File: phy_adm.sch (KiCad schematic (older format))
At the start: 28 parts

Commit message: sch: Add misc doc texts
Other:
- note added: "PHY reference clock"
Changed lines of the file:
@@
 Wire Wire Line
 	4500 5500 4500 5750
+Text Notes 4800 6400 0    50   ~ 0
+PHY reference clock
 $EndSCHEMATC

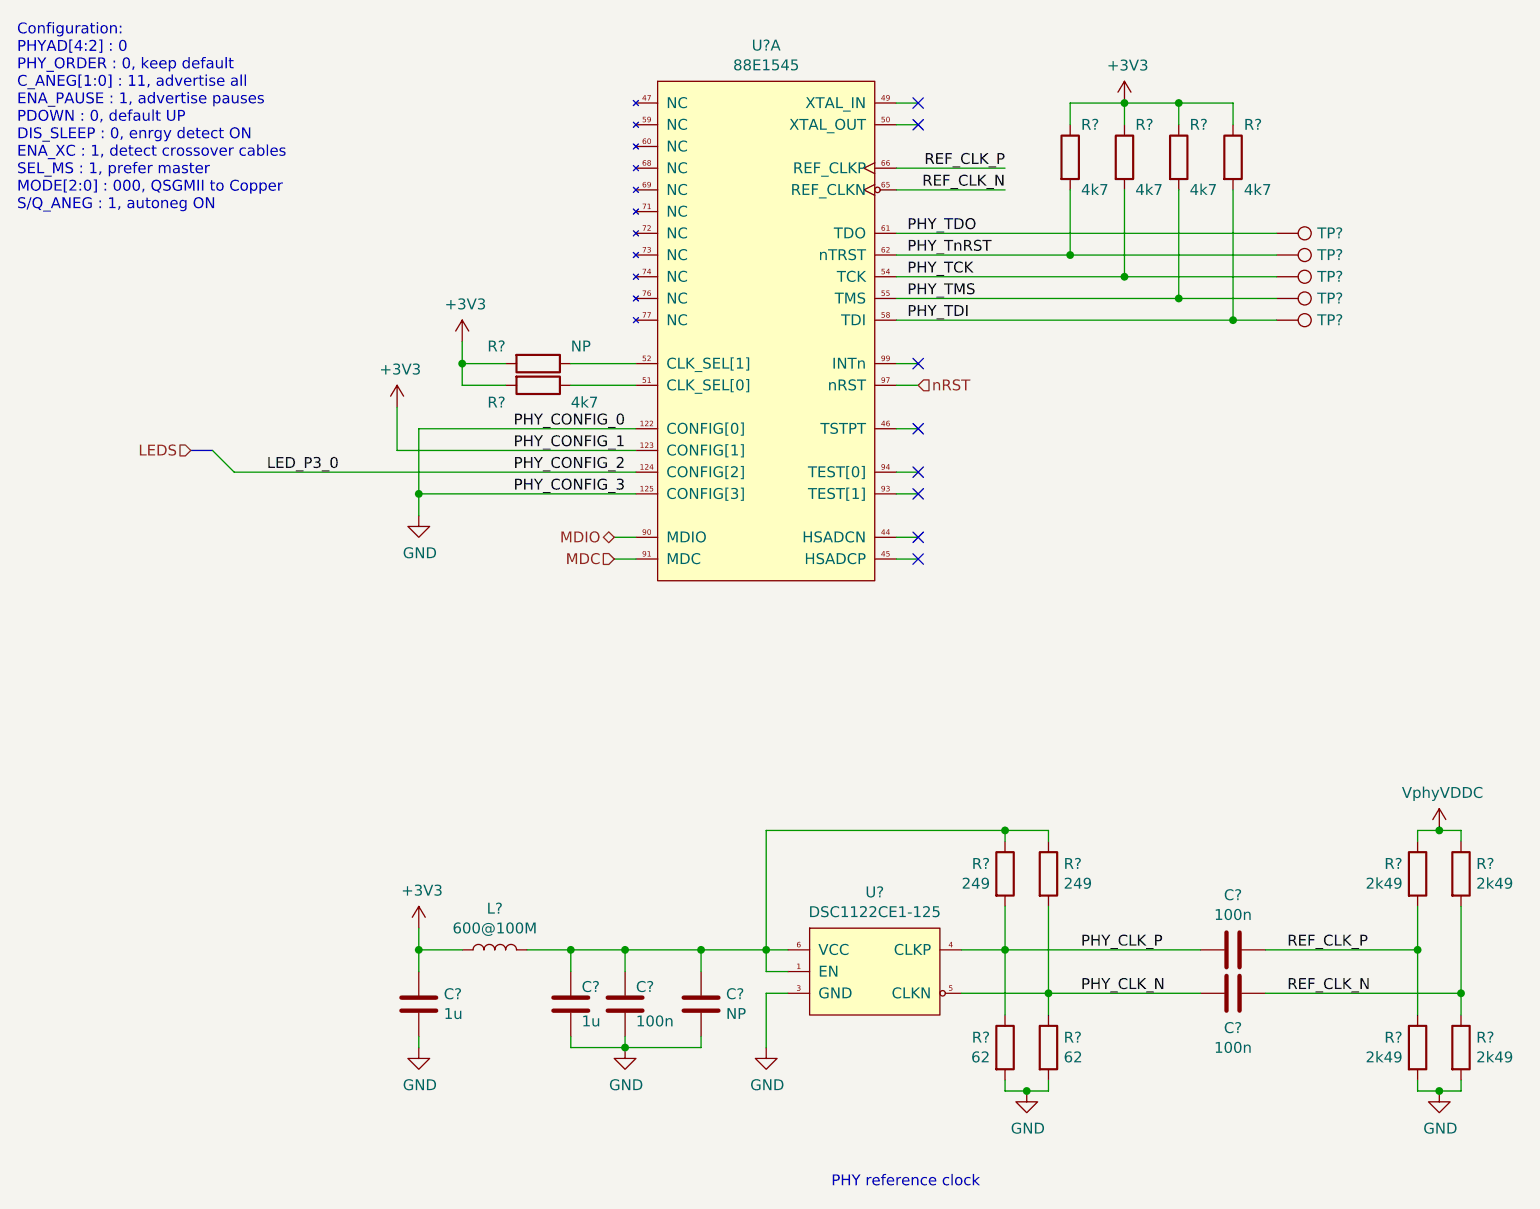
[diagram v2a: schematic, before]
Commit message: sch: Replace regular symbols with small variant
Done for most capacitors and resistors
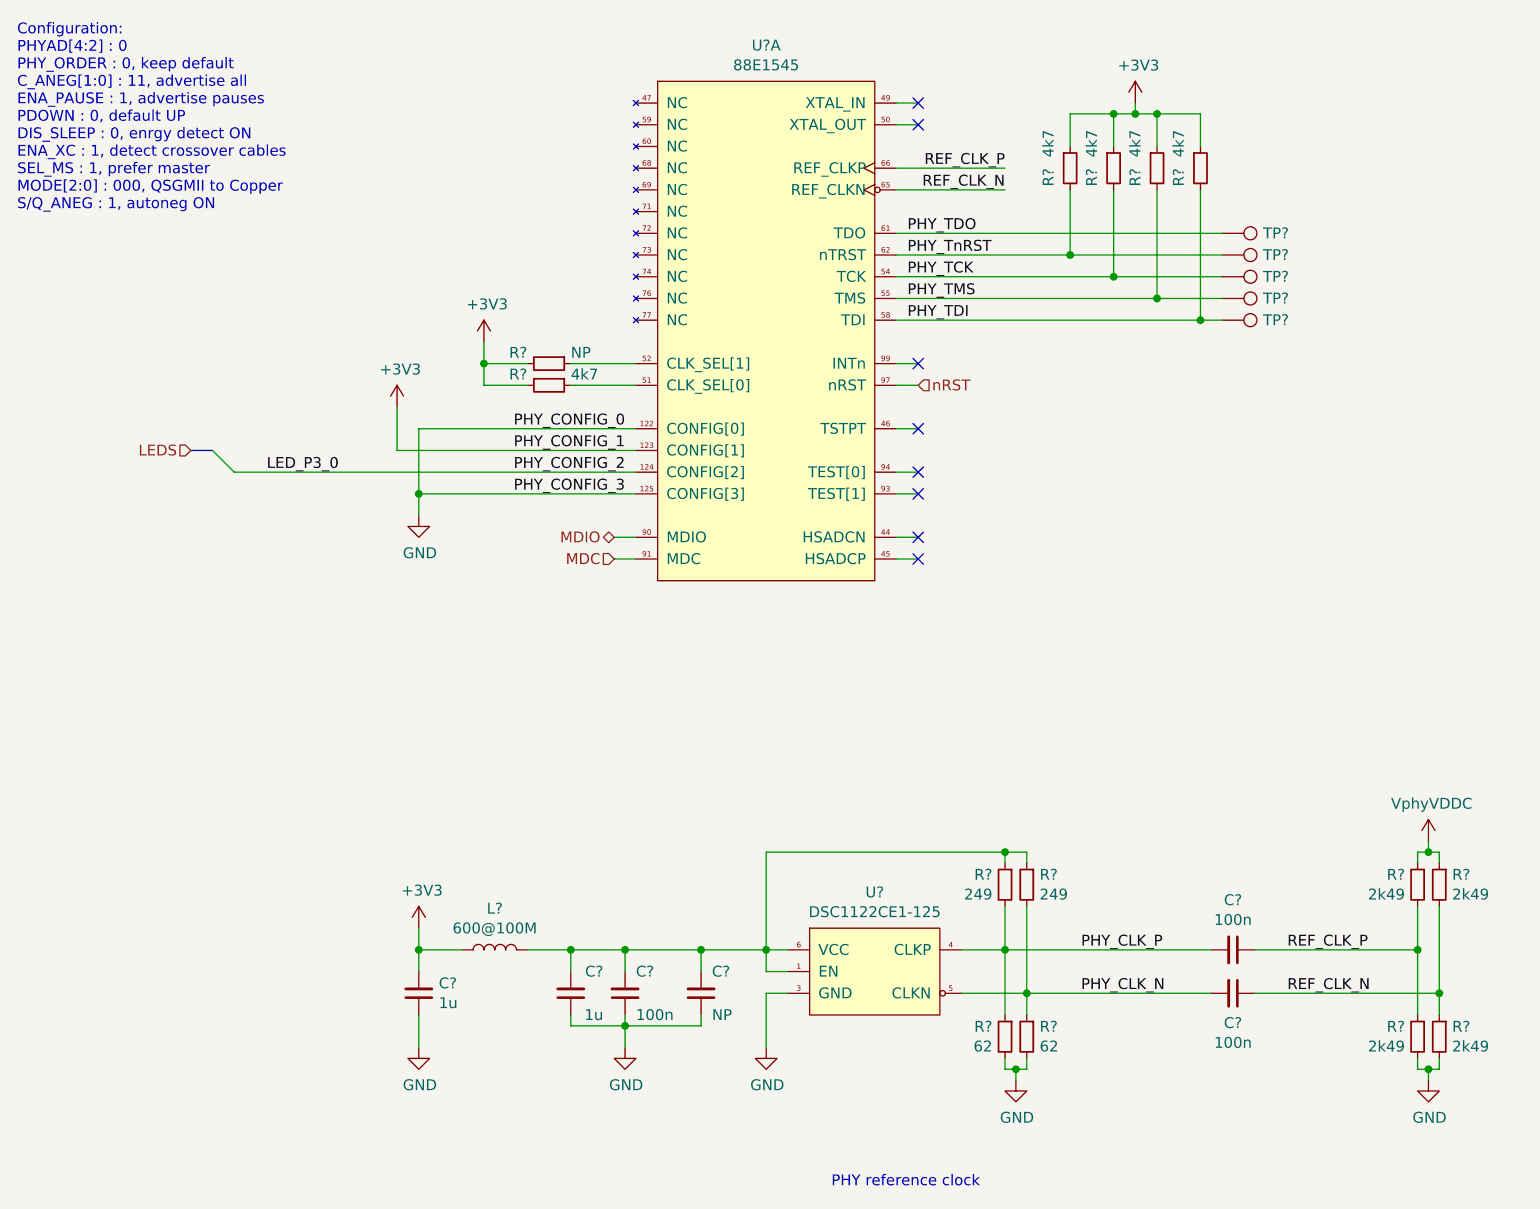
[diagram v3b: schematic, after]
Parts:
- removed C?: NP, symbol Device:C
- removed C? (x3): 100n, symbol Device:C
- removed C? (x2): 1u, symbol Device:C
- removed R? (x2): 249, symbol Device:R
- removed R? (x2): 62, symbol Device:R
- removed R? (x4): 2k49, symbol Device:R
- removed R? (x5): 4k7, symbol Device:R
- removed R?: NP, symbol Device:R
- added C? (x3): 100n, symbol Device:C_Small
- added C?: NP, symbol Device:C_Small
- added C? (x2): 1u, symbol Device:C_Small
- added R? (x5): 4k7, symbol Device:R_Small
- added R?: NP, symbol Device:R_Small
- added R? (x2): 249, symbol Device:R_Small
- added R? (x2): 62, symbol Device:R_Small
- added R? (x4): 2k49, symbol Device:R_Small
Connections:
- net +3V3: now also C?.2, R?.1, R?.1, R?.1, R?.1, R?.2, R?.2
- net GND: now also C?.1, C?.1, C?.1, C?.1, R?.2, R?.2, R?.2, R?.2
- net PHY_CLK_N: now also C?.2, R?.1, R?.2
- net PHY_CLK_P: now also C?.2, R?.1, R?.2
- net PHY_TCK: now also R?.2
- net PHY_TDI: now also R?.2
- net PHY_TMS: now also R?.2
- net PHY_TnRST: now also R?.2
- net REF_CLK_N: now also C?.1, R?.1, R?.2
- net REF_CLK_P: now also C?.1, R?.1, R?.2
- net VphyVDDC: now also R?.1, R?.1
- net at U?.51 (CLK_SEL[0]): now also R?.1
- net at U?.52 (CLK_SEL[1]): now also R?.1
- net at L?.2, U?.1 (EN), U?.6 (VCC): now also C?.2, C?.2, C?.2, R?.1, R?.1
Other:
- moved on the sheet: TP?

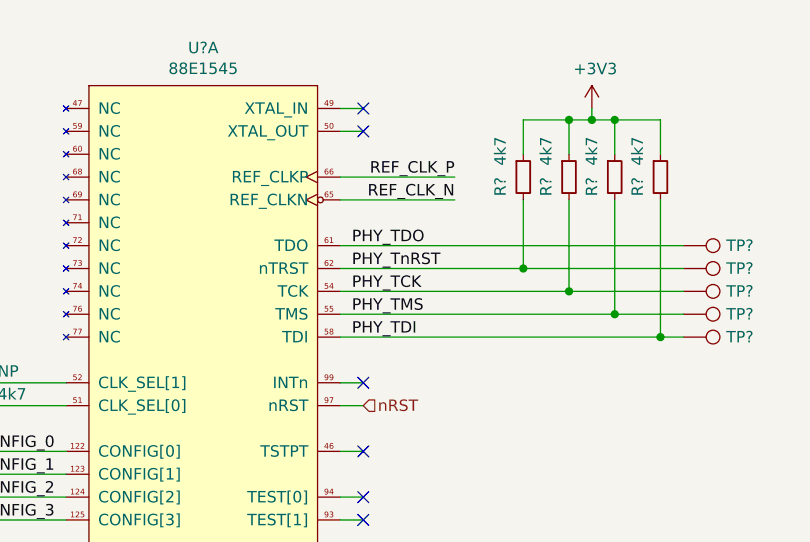
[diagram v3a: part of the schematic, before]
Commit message: sch: Misc fixes
- add missing NC on PCIe switch
- fix incorrect cap values on PCIe supply
- fix main schematic interco labels
- fix PHY JTAG signal name
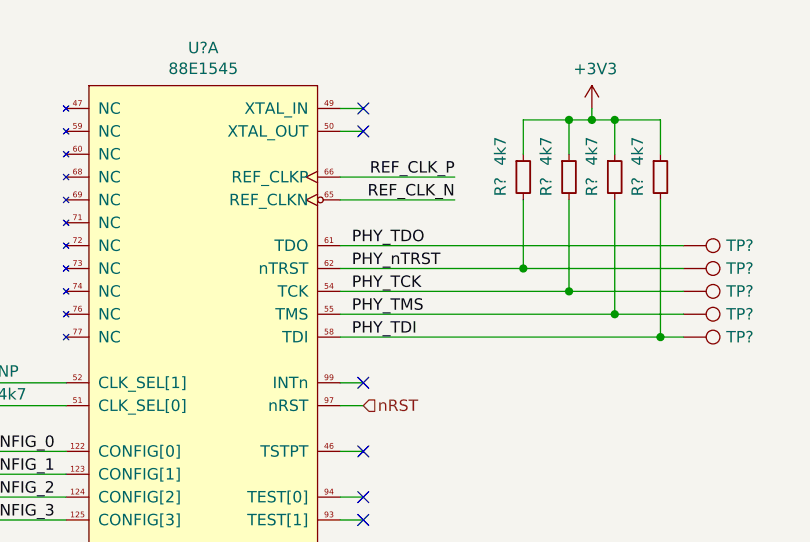
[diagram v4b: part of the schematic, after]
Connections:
- net PHY_TnRST renamed PHY_nTRST
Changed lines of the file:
@@
 PHY_TDO
 Text Label 5150 2100 0    50   ~ 0
-PHY_TnRST
+PHY_nTRST
 Text Label 5150 2200 0    50   ~ 0
 PHY_TCK

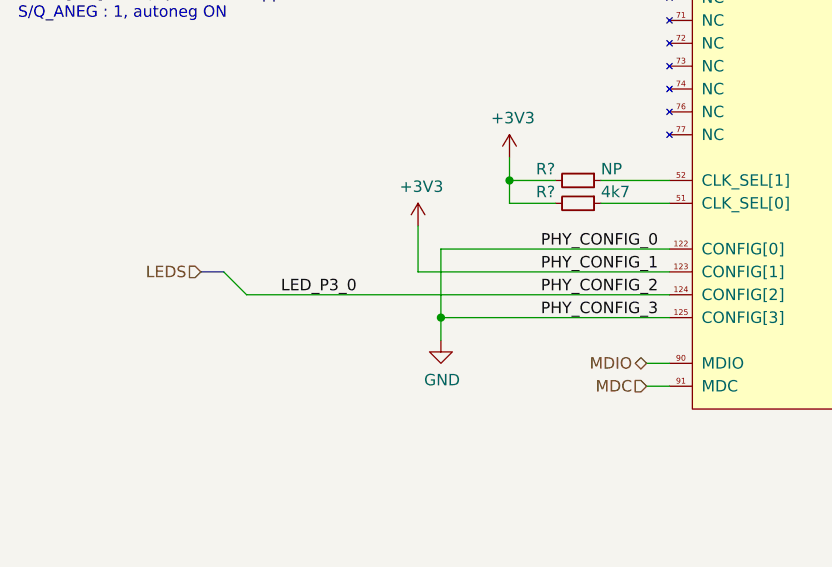
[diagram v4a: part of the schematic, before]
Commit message: sch: Remove ALL busses since kicad's support is broken
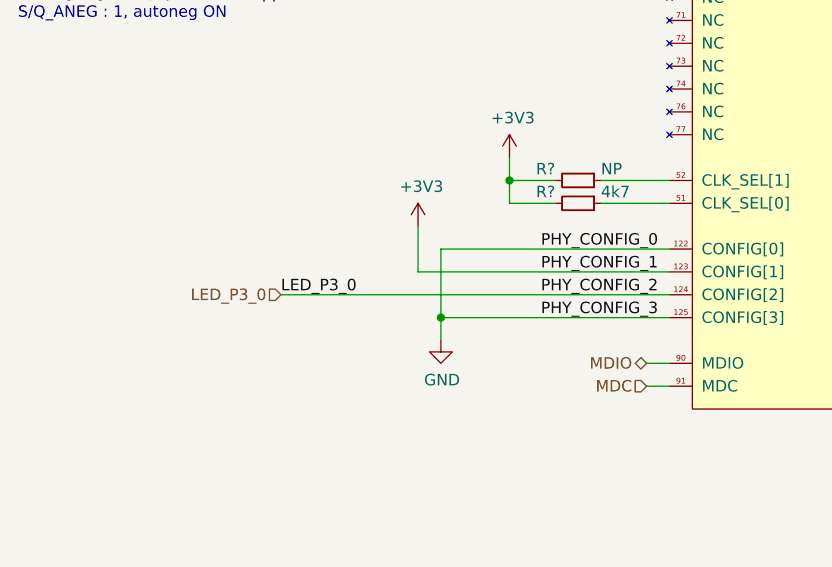
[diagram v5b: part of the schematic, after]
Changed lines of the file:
@@
 	2900 3200 2900 3300
 Wire Wire Line
-	2050 3100 3900 3100
-Wire Bus Line
-	1950 3000 1850 3000
-Entry Wire Line
-	1950 3000 2050 3100
-Text HLabel 1850 3000 0    50   Input ~ 0
-LEDS
+	2200 3100 3900 3100
 Text Notes 1050 1900 0    50   ~ 0
 Configuration:\nPHYAD[4:2] : 0\nPHY_ORDER : 0, keep default\nC_ANEG[1:0] : 11, advertise all\nENA_PAUSE : 1, advertise pauses\nPDOWN : 0, default UP\nDIS_SLEEP : 0, enrgy detect ON\nENA_XC : 1, detect crossover cables\nSEL_MS : 1, prefer master\nMODE[2:0] : 000, QSGMII to Copper\nS/Q_ANEG : 1, autoneg ON
@@
 	-1   0    0    1
 $EndComp
+Text HLabel 2200 3100 0    50   Input ~ 0
+LED_P3_0
 $EndSCHEMATC

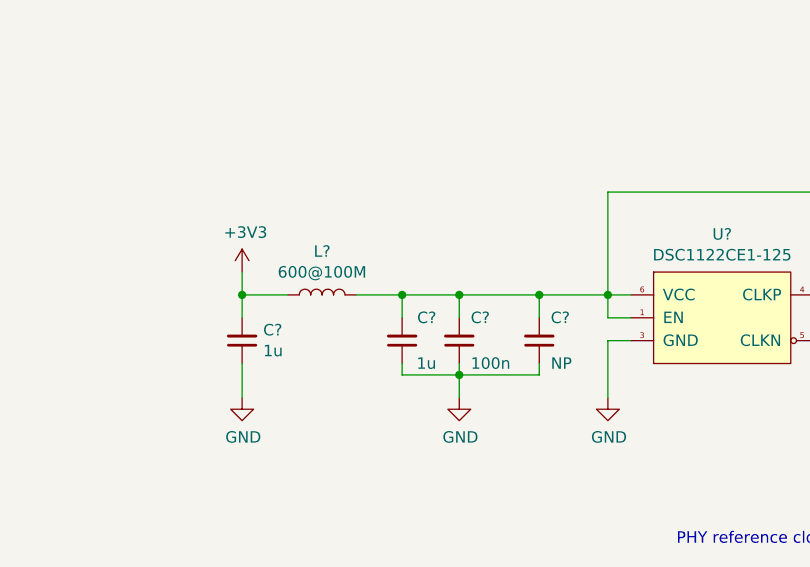
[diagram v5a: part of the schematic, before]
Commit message: lib, sch: Misc changes to make ERC happy
- add resistors to PCIe switch GPIOs
- add NC flags on PHY unused LED outputs
- add dummy supply on Earth PSU
- add dummy supply on PHY ref clock's VCC
- LTC3633: deduplicate SW1/2 outputs
- ILS8033: deduplicate LX1/2 and PGND1/2 outputs
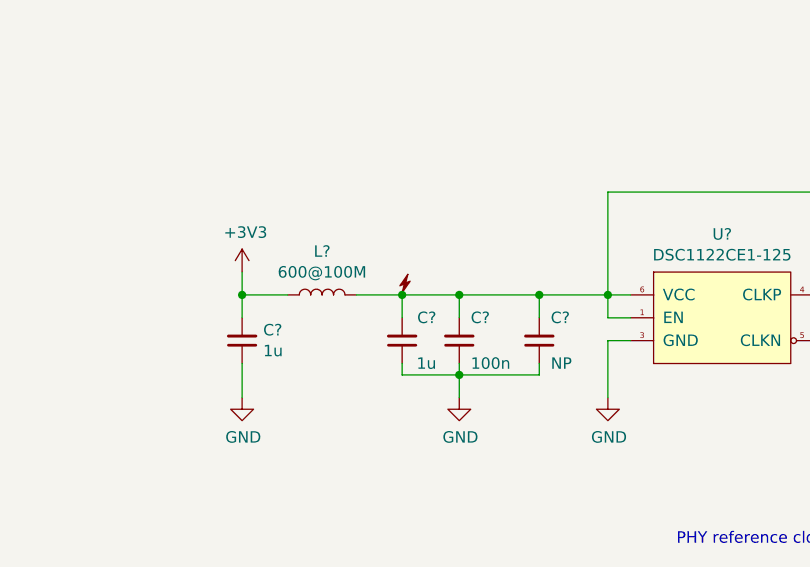
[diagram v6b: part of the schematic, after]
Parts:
- added DS?: DummySupply, symbol pimouss-motherboard:DummySupply
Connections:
- net at C?.2, C?.2, C?.2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: now also DS?.~ (Dummy)
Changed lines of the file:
@@
 Text HLabel 2200 3100 0    50   Input ~ 0
 LED_P3_0
+$Comp
+L pimouss-motherboard:DummySupply DS?
+U 1 1 5E49E098
+P 3600 5300
+F 0 "DS?" H 3600 5300 50  0001 C CNN
+F 1 "DummySupply" H 3600 5300 50  0001 C CNN
+F 2 "" H 3600 5300 50  0001 C CNN
+F 3 "" H 3600 5300 50  0001 C CNN
+	1    3600 5300
+	1    0    0    -1
+$EndComp
 $EndSCHEMATC
